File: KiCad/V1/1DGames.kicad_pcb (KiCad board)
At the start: 2 copper layers, 100 x 70 mm, 12 parts, among them Q1 AO3401A, Q2 AO3401A, Q3 AO3401A, Q4 AO3401A, U1 ESP32-DEVKITC-32D

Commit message: Compilable for Arduino Uno
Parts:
- removed Q3, Q4: AO3401A, Package_TO_SOT_SMD:SOT-23
- removed RN1: 10K, Resistor_THT:R_Array_SIP9
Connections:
- net /LED_STRIP_RED_DATA renamed /LED_STRIP_DATA
- net /LED_STRIP_RED_DRAIN renamed /LED_STRIP_DRAIN
- net /P1_DISP_CLK renamed /LED_SEGMENTS_CLK
- net /P1_DISP_DIN renamed /LED_SEGMENTS_DIN
- U1 pad 27: /BUTTONS_PARALLEL_LOAD_INPUT -> unconnected-(U1-Pad27)
- U1 pad 28: /BUTTONS_CLOCK_INPUT -> unconnected-(U1-Pad28)
- U1 pad 29: /BUTTONS_SERIAL_OUTPUT -> unconnected-(U1-Pad29)
- U1 pad 31: /LED_STRIP_BLUE_DATA -> unconnected-(U1-Pad31)
- U1 pad 32: /LED_STRIP_GREEN_DATA -> unconnected-(U1-Pad32)

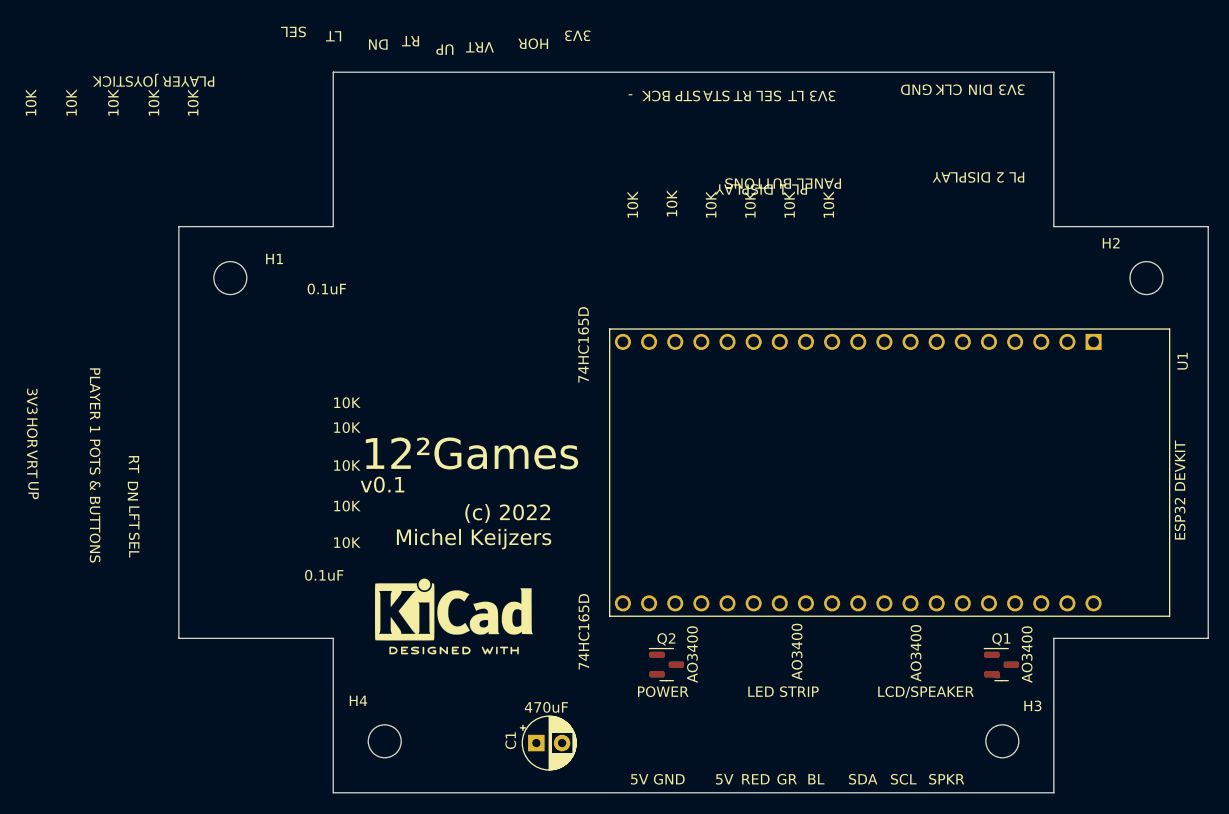
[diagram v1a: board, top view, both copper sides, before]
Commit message: Electronic scheme, program for calculating LED coordinates.
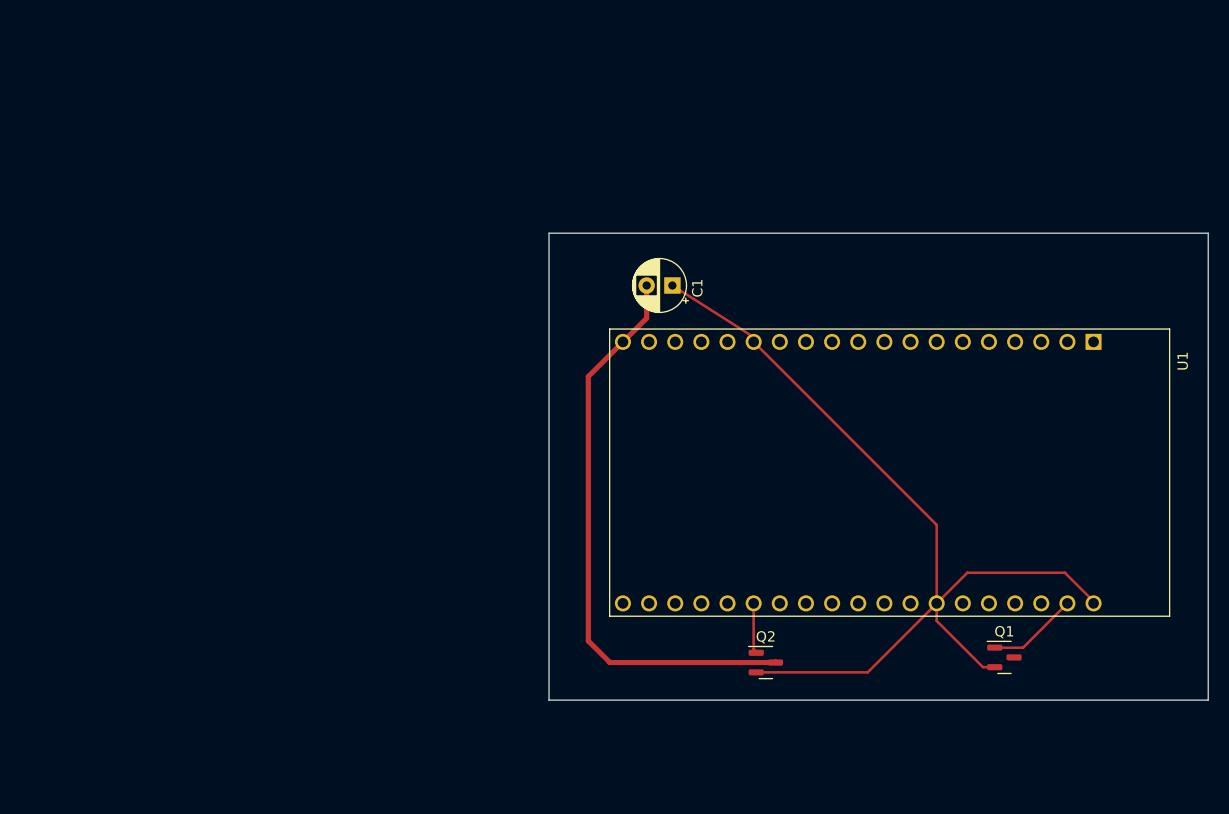
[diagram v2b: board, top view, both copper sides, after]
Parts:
- removed H1, H2, H3, H4: MountingHole, MountingHole:MountingHole_3.2mm_M3
- removed REF**: KiCad-Logo2_6mm_SilkScreen, Symbol:KiCad-Logo2_6mm_SilkScreen
- moved C1 46.4 mm to (72.9, 45.7), turned to 180 degrees
- moved Q2 9.64 mm to (82.0, 82.3)
- moved Q1 0.75 mm to (105.2, 81.8)
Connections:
- net /PANEL_SELECT_BUTTON renamed /PANEL_START_STOP_BUTTON
- Q2 pad 3: /LED_STRIP_DRAIN -> /+5V
- U1 pad 10: /PANEL_RIGHT_BUTTON -> unconnected-(U1-Pad10)
- U1 pad 11: /PANEL_START_BUTTON -> /PANEL_RIGHT_BUTTON
- U1 pad 12: /PANEL_STOP_BUTTON -> unconnected-(U1-Pad12)
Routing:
- net GND: track 0.30 -> 90.2 mm
- net /+5V: track 0.00 -> 56.0 mm
- net /SPEAKER_IN: track 0.00 -> 8.84 mm
- net /LED_STRIP_DATA: track 0.00 -> 5.06 mm
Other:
- board size 100 x 70 mm -> 64 x 45.4 mm
- board text removed: "(c) 2022 Michel Keijzers"
- board text removed: "-"
- board text removed: "0.1uF"
- board text removed: "10K"
- board text removed: "12²Games"
- board text removed: "3V3"
- board text removed: "470uF"
- board text removed: "5V"
- board text removed: "74HC165D"
- board text removed: "AO3400"
- board text removed: "BCK"
- board text removed: "BL"
- board text removed: "CLK"
- board text removed: "DIN"
- board text removed: "DN"
- board text removed: "ESP32 DEVKIT"
- board text removed: "GND"
- board text removed: "GR"
- board text removed: "HOR"
- board text removed: "LCD/SPEAKER"
- board text removed: "LED STRIP"
- board text removed: "LFT"
- board text removed: "LT"
- board text removed: "PANEL BUTTONS"
- board text removed: "PL 1 DISPLAY"
- board text removed: "PL 2 DISPLAY"
- board text removed: "PLAYER 1 POTS & BUTTONS"
- board text removed: "PLAYER JOYSTICK"
- board text removed: "POWER"
- board text removed: "RED"
- board text removed: "RT"
- board text removed: "SCL"
- board text removed: "SDA"
- board text removed: "SEL"
- board text removed: "SPKR"
- board text removed: "STA"
- board text removed: "STP"
- board text removed: "UP"
- board text removed: "VRT"
- board text removed: "v0.1"

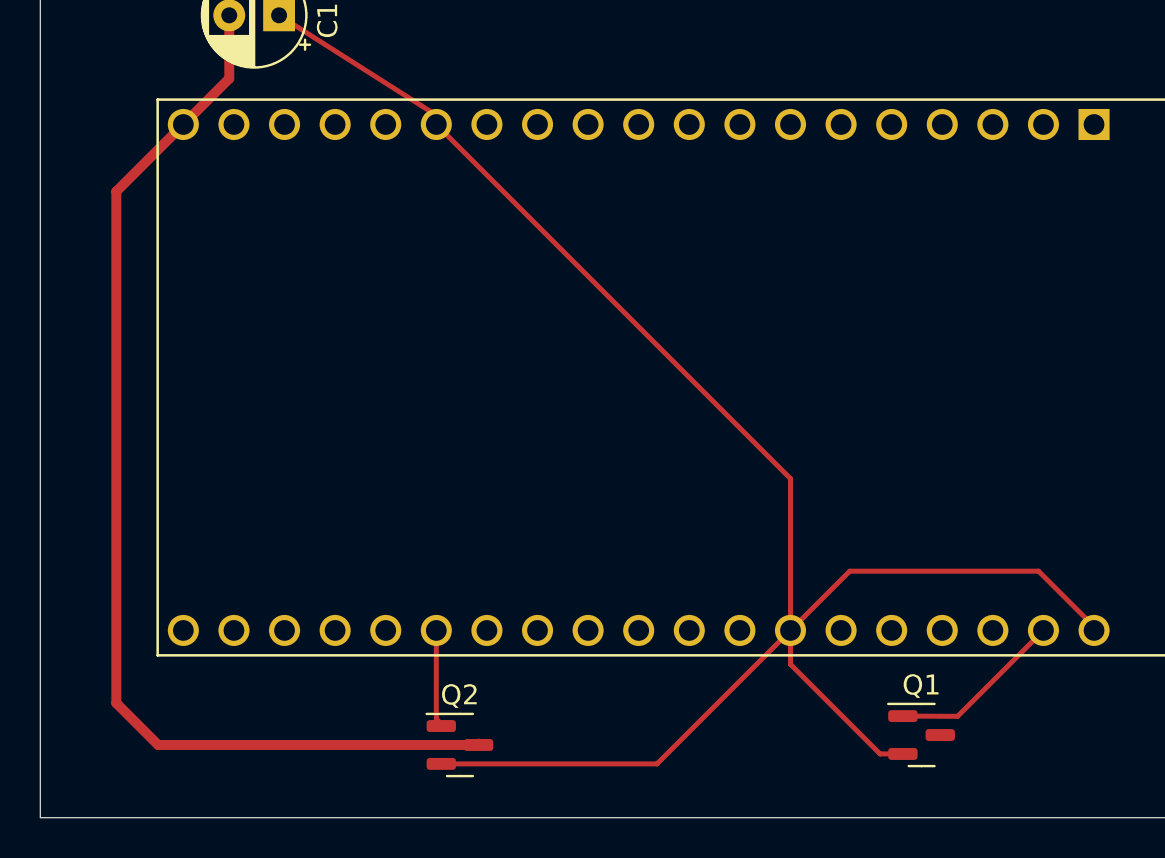
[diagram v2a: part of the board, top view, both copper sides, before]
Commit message: Fixed sound/buttons.
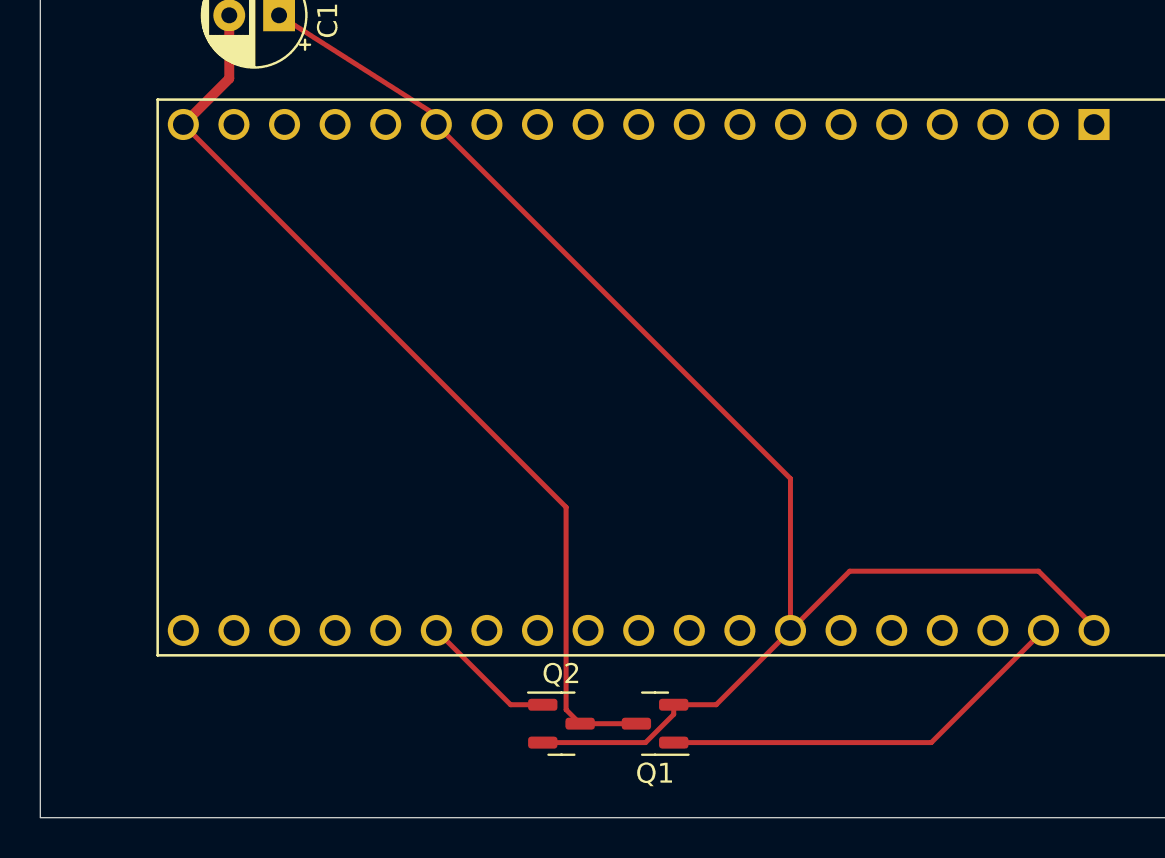
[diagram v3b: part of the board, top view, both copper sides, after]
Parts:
- moved Q1 13.4 mm to (91.8, 81.3), turned to 180 degrees
- moved Q2 5.21 mm to (87.1, 81.3)
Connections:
- Q1 pad 3: /SPEAKER_DRAIN -> /+5V
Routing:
- net GND: track 90.2 -> 75.7 mm
- net /SPEAKER_IN: track 8.84 -> 20.9 mm
- net /+5V: track 56.0 -> 47.6 mm
- net /LED_STRIP_DATA: track 5.06 -> 6.89 mm
